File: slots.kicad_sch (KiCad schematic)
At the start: 6 parts

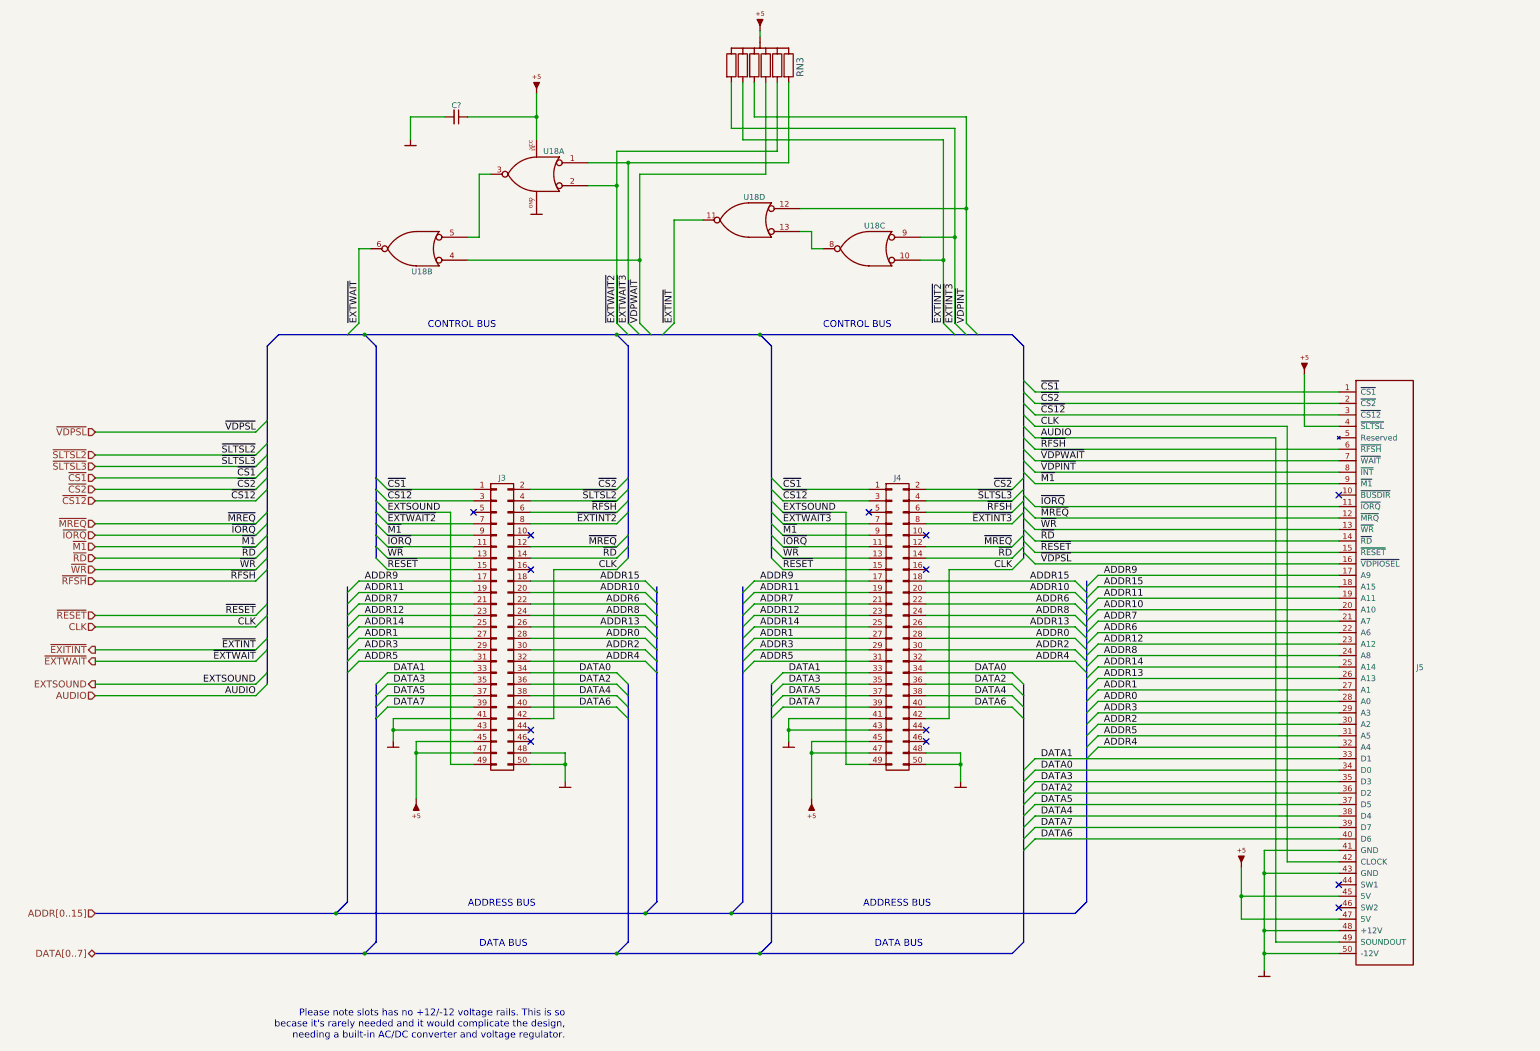
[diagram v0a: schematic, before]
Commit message: Fix wrong cap type in clock generator
Also fill some references automatically generated by KiCAD.
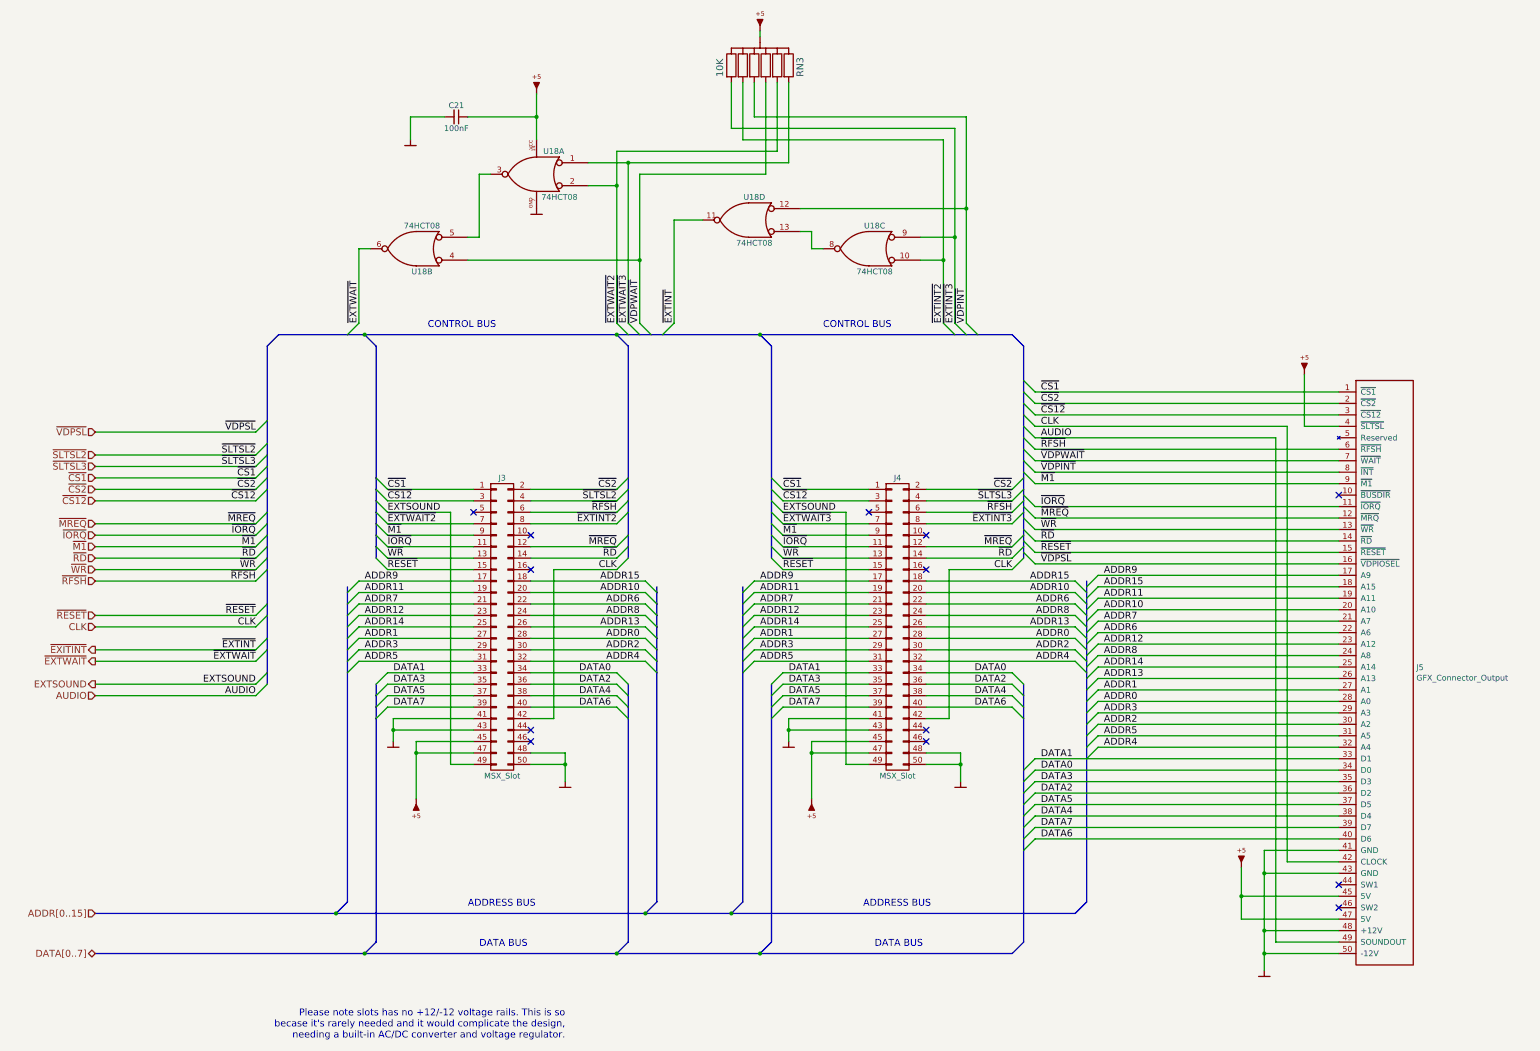
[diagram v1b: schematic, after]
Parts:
- C21: renamed from C?; value (none) -> 100nF; footprint (none) -> artemisa:Disc_capacitor
- J3, J4: value (none) -> MSX_Slot; footprint (none) -> artemisa:Slot_conn
- J5: value (none) -> GFX_Connector_Output; footprint (none) -> artemisa:GFX_conn
- RN3: value (none) -> 10K; footprint (none) -> artemisa:RN6
- U18: value (none) -> 74HCT08; footprint (none) -> artemisa:DIP-14_300
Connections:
- net VCC: now also C21.1, J3.45 (Pin_45), J3.47 (Pin_47), J4.45 (Pin_45), J4.47 (Pin_47), J5.4 (~{SLTSL}), J5.45 (5V), J5.47 (5V), RN3.1, U18.14 (VCC)
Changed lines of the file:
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@@
     (in_bom yes) (on_board yes)
     (property "Reference" "J3" (id 0) (at 165.1 129.54 0))
-    (property "Value" "" (id 1) (at 165.1 195.58 0))
-    (property "Footprint" "" (id 2) (at 163.83 162.56 0)
+    (property "Value" "MSX_Slot" (id 1) (at 165.1 195.58 0))
+    (property "Footprint" "artemisa:Slot_conn" (id 2) (at 163.83 162.56 0)
       (effects (font (size 1.27 1.27)) hide)
     )
@@
     (in_bom yes) (on_board yes)
     (property "Reference" "J4" (id 0) (at 252.73 129.54 0))
-    (property "Value" "" (id 1) (at 252.73 195.58 0))
-    (property "Footprint" "" (id 2) (at 251.46 162.56 0)
+    (property "Value" "MSX_Slot" (id 1) (at 252.73 195.58 0))
+    (property "Footprint" "artemisa:Slot_conn" (id 2) (at 251.46 162.56 0)
       (effects (font (size 1.27 1.27)) hide)
     )
@@
       (effects (font (size 1.27 1.27)) (justify right))
     )
-    (property "Value" "" (id 1) (at 367.7158 173.863 0)
+    (property "Value" "GFX_Connector_Output" (id 1) (at 367.7158 173.863 0)
       (effects (font (size 1.27 1.27)) (justify right))
     )
-    (property "Footprint" "" (id 2) (at 367.03 146.05 0)
+    (property "Footprint" "artemisa:GFX_conn" (id 2) (at 367.03 146.05 0)
       (effects (font (size 1.27 1.27)) hide)
     )
@@
       (effects (font (size 1.524 1.524)) hide)
     )
-    (property "Value" "" (id 1) (at 328.93 210.82 0)
+    (property "Value" "VCC" (id 1) (at 328.93 210.82 0)
       (effects (font (size 1.524 1.524)) hide)
     )
@@
       (effects (font (size 1.524 1.524)) hide)
     )
-    (property "Value" "" (id 1) (at 334.01 236.22 0)
+    (property "Value" "GND" (id 1) (at 334.01 236.22 0)
       (effects (font (size 1.524 1.524)) hide)
     )
@@
       (effects (font (size 1.524 1.524)) hide)
     )
-    (property "Value" "" (id 1) (at 266.7 194.31 0)
+    (property "Value" "GND" (id 1) (at 266.7 194.31 0)
       (effects (font (size 1.524 1.524)) hide)
     )
@@
       (effects (font (size 1.524 1.524)) hide)
     )
-    (property "Value" "" (id 1) (at 233.68 205.74 0)
+    (property "Value" "VCC" (id 1) (at 233.68 205.74 0)
       (effects (font (size 1.524 1.524)) hide)
     )
@@
       (effects (font (size 1.524 1.524)) hide)
     )
-    (property "Value" "" (id 1) (at 228.6 185.42 0)
+    (property "Value" "GND" (id 1) (at 228.6 185.42 0)
       (effects (font (size 1.524 1.524)) hide)
     )
@@
       (effects (font (size 1.524 1.524)) hide)
     )
-    (property "Value" "" (id 1) (at 179.07 194.31 0)
+    (property "Value" "GND" (id 1) (at 179.07 194.31 0)
       (effects (font (size 1.524 1.524)) hide)
     )
@@
       (effects (font (size 1.524 1.524)) hide)
     )
-    (property "Value" "" (id 1) (at 146.05 205.74 0)
+    (property "Value" "VCC" (id 1) (at 146.05 205.74 0)
       (effects (font (size 1.524 1.524)) hide)
     )
@@
       (effects (font (size 1.524 1.524)) hide)
     )
-    (property "Value" "" (id 1) (at 140.97 185.42 0)
+    (property "Value" "GND" (id 1) (at 140.97 185.42 0)
       (effects (font (size 1.524 1.524)) hide)
     )
@@
       (effects (font (size 1.524 1.524)) hide)
     )
-    (property "Value" "" (id 1) (at 222.25 24.13 0)
+    (property "Value" "VCC" (id 1) (at 222.25 24.13 0)
       (effects (font (size 1.524 1.524)) hide)
     )
@@
       (effects (font (size 1.524 1.524)) (justify left))
     )
-    (property "Value" "" (id 1) (at 213.36 40.64 90)
+    (property "Value" "10K" (id 1) (at 213.36 40.64 90)
       (effects (font (size 1.524 1.524)) (justify left))
     )
-    (property "Footprint" "" (id 2) (at 219.71 40.005 0)
+    (property "Footprint" "artemisa:RN6" (id 2) (at 219.71 40.005 0)
       (effects (font (size 1.524 1.524)) hide)
     )
@@
     (in_bom yes) (on_board yes)
     (property "Reference" "U18" (id 0) (at 176.53 57.15 0))
-    (property "Value" "" (id 1) (at 177.8 67.31 0))
-    (property "Footprint" "" (id 2) (at 182.88 60.325 0)
+    (property "Value" "74HCT08" (id 1) (at 177.8 67.31 0))
+    (property "Footprint" "artemisa:DIP-14_300" (id 2) (at 182.88 60.325 0)
       (effects (font (size 1.27 1.27)) hide)
     )
@@
     (in_bom yes) (on_board yes)
     (property "Reference" "U18" (id 0) (at 147.32 83.82 0))
-    (property "Value" "" (id 1) (at 147.32 73.66 0))
-    (property "Footprint" "" (id 2) (at 156.21 80.645 0)
+    (property "Value" "74HCT08" (id 1) (at 147.32 73.66 0))
+    (property "Footprint" "artemisa:DIP-14_300" (id 2) (at 156.21 80.645 0)
       (effects (font (size 1.27 1.27)) hide)
     )
@@
     (in_bom yes) (on_board yes)
     (property "Reference" "U18" (id 0) (at 247.65 73.66 0))
-    (property "Value" "" (id 1) (at 247.65 83.82 0))
-    (property "Footprint" "" (id 2) (at 256.54 76.835 0)
+    (property "Value" "74HCT08" (id 1) (at 247.65 83.82 0))
+    (property "Footprint" "artemisa:DIP-14_300" (id 2) (at 256.54 76.835 0)
       (effects (font (size 1.27 1.27)) hide)
     )
@@
     (in_bom yes) (on_board yes)
     (property "Reference" "U18" (id 0) (at 220.98 67.31 0))
-    (property "Value" "" (id 1) (at 220.98 77.47 0))
-    (property "Footprint" "" (id 2) (at 229.87 70.485 0)
+    (property "Value" "74HCT08" (id 1) (at 220.98 77.47 0))
+    (property "Footprint" "artemisa:DIP-14_300" (id 2) (at 229.87 70.485 0)
       (effects (font (size 1.27 1.27)) hide)
     )
@@
       (effects (font (size 1.524 1.524)) hide)
     )
-    (property "Value" "" (id 1) (at 342.9 100.33 0)
+    (property "Value" "VCC" (id 1) (at 342.9 100.33 0)
       (effects (font (size 1.524 1.524)) hide)
     )
@@
   (symbol (lib_id "artemisa:GND") (at 172.72 69.85 0) (unit 1)
     (in_bom yes) (on_board yes)
-    (property "Reference" "#PWR?" (id 0) (at 172.72 72.39 0)
-      (effects (font (size 1.524 1.524)) hide)
-    )
-    (property "Value" "" (id 1) (at 172.72 67.31 0)
+    (property "Reference" "#PWR0164" (id 0) (at 172.72 72.39 0)
+      (effects (font (size 1.524 1.524)) hide)
+    )
+    (property "Value" "GND" (id 1) (at 172.72 67.31 0)
       (effects (font (size 1.524 1.524)) hide)
     )
@@
   (symbol (lib_id "artemisa:VCC") (at 172.72 44.45 0) (unit 1)
     (in_bom yes) (on_board yes)
-    (property "Reference" "#PWR?" (id 0) (at 172.72 45.72 0)
-      (effects (font (size 1.524 1.524)) hide)
-    )
-    (property "Value" "" (id 1) (at 172.72 38.1 0)
+    (property "Reference" "#PWR0165" (id 0) (at 172.72 45.72 0)
+      (effects (font (size 1.524 1.524)) hide)
+    )
+    (property "Value" "VCC" (id 1) (at 172.72 38.1 0)
       (effects (font (size 1.524 1.524)) hide)
     )
@@
   (symbol (lib_id "artemisa:Cap") (at 154.94 49.53 270) (unit 1)
     (in_bom yes) (on_board yes)
-    (property "Reference" "C?" (id 0) (at 154.94 46.99 90))
-    (property "Value" "" (id 1) (at 154.94 52.07 90))
-    (property "Footprint" "" (id 2) (at 154.94 49.53 0)
+    (property "Reference" "C21" (id 0) (at 154.94 46.99 90))
+    (property "Value" "100nF" (id 1) (at 154.94 52.07 90))
+    (property "Footprint" "artemisa:Disc_capacitor" (id 2) (at 154.94 49.53 0)
       (effects (font (size 1.27 1.27)) hide)
     )
@@
   (symbol (lib_id "artemisa:GND") (at 144.78 54.61 0) (unit 1)
     (in_bom yes) (on_board yes)
-    (property "Reference" "#PWR?" (id 0) (at 144.78 57.15 0)
-      (effects (font (size 1.524 1.524)) hide)
-    )
-    (property "Value" "" (id 1) (at 144.78 52.07 0)
-      (effects (font (size 1.524 1.524)) hide)
-    )
+    (property "Reference" "#PWR0178" (id 0) (at 144.78 57.15 0)
+      (effects (font (size 1.524 1.524)) hide)
+    )
+    (property "Value" "GND" (id 1) (at 144.78 52.07 0)
+      (effects (font (size 1.524 1.524)) hide)
+    )
